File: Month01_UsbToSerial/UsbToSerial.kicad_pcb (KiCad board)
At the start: 2 copper layers, 14 parts, among them J1 USB_B_Micro, J2 Conn1, J3 Conn2, U1 FT232RL

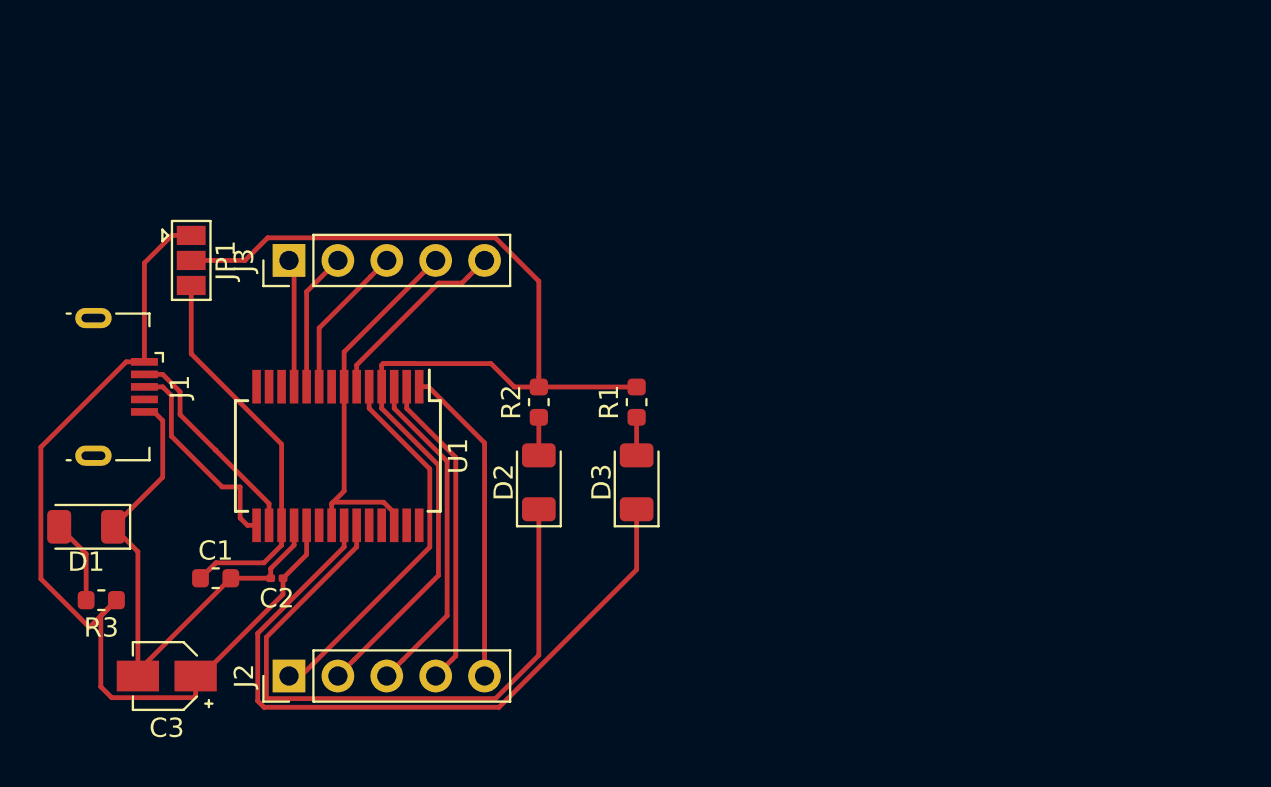
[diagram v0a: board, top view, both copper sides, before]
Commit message: added files from mistaken working copy in separate folder
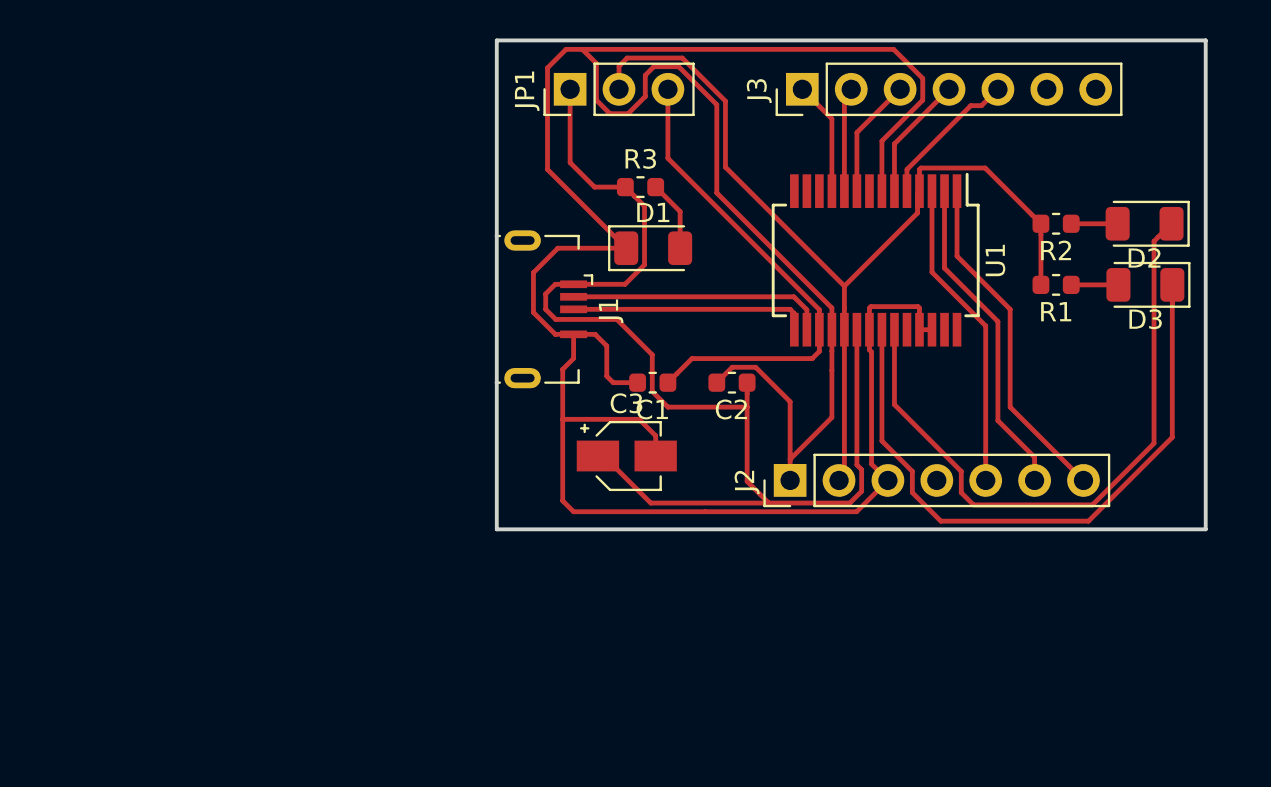
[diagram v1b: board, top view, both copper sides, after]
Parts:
- C2: footprint Capacitor_SMD:C_0201_0603Metric -> Capacitor_SMD:C_0603_1608Metric
- J2: value Conn1 -> Conn_01x07_Female; footprint Connector_PinHeader_2.54mm:PinHeader_1x05_P2.54mm_Vertical -> Connector_PinHeader_2.54mm:PinHeader_1x07_P2.54mm_Vertical
- J3: value Conn2 -> Conn_01x07_Female; footprint Connector_PinHeader_2.54mm:PinHeader_1x05_P2.54mm_Vertical -> Connector_PinHeader_2.54mm:PinHeader_1x07_P2.54mm_Vertical
- JP1: footprint Jumper:SolderJumper-3_P1.3mm_Open_Pad1.0x1.5mm -> Connector_PinHeader_2.54mm:PinHeader_1x03_P2.54mm_Vertical
- moved R3 35.3 mm to (84.3, 74.9), turned to 0 degrees
- moved D2 34.2 mm to (110.5, 76.8), turned to 180 degrees
- moved D1 32.8 mm to (85.0, 78.1), turned to 0 degrees
- moved U1 29.7 mm to (96.5, 78.7)
- moved R2 28.4 mm to (105.9, 76.8), turned to 180 degrees
- moved D3 28.3 mm to (110.5, 80.0), turned to 180 degrees
- moved J3 28.1 mm to (92.7, 69.8)
- moved J2 27.9 mm to (92.1, 90.2)
- moved C3 26.5 mm to (83.6, 88.9), turned to 0 degrees
- moved C2 25.7 mm to (89.1, 85.1)
- moved C1 24.9 mm to (84.9, 85.1), turned to 180 degrees
- moved J1 22.7 mm to (79.4, 81.3)
- moved R1 22.6 mm to (105.9, 80.0), turned to 180 degrees
- moved JP1 21.6 mm to (80.6, 69.8), turned to 90 degrees
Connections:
- J2 pad 1: RXI -> GNDREF
- J2 pad 3: RTS -> GNDREF
- J2 pad 4: DTR -> Net-(J2-Pad4)
- J2 pad 5: TX0 -> RTS
- J3 pad 4: GNDREF -> RI
- J3 pad 5: RI -> RXI
- U1 pad 19: +5V -> PWR
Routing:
- net GNDREF: track 48.5 -> 143.0 mm
- net +5V: track 49.2 -> 62.1 mm
- net RXI: track 19.7 -> 7.58 mm
- net PWR: track 59.9 -> 48.6 mm
- net +3V3: track 20.4 -> 25.4 mm
- net Net-(D3-Pad1): track 36.9 -> 33.0 mm
- net RI: track 10.0 -> 6.46 mm
- net Net-(J1-Pad2): track 11.1 -> 13.4 mm
- net DCD: track 7.23 -> 5.44 mm
- net DCR: track 8.02 -> 6.22 mm
- net Net-(J1-Pad3): track 11.0 -> 12.4 mm
- net RTS: track 17.5 -> 16.2 mm
- net TX0: track 16.7 -> 17.8 mm
- net CTS: track 6.67 -> 5.93 mm
- net Net-(D1-Pad2): track 4.39 -> 3.70 mm
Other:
- board outline added: 36.8 x 25.4 mm

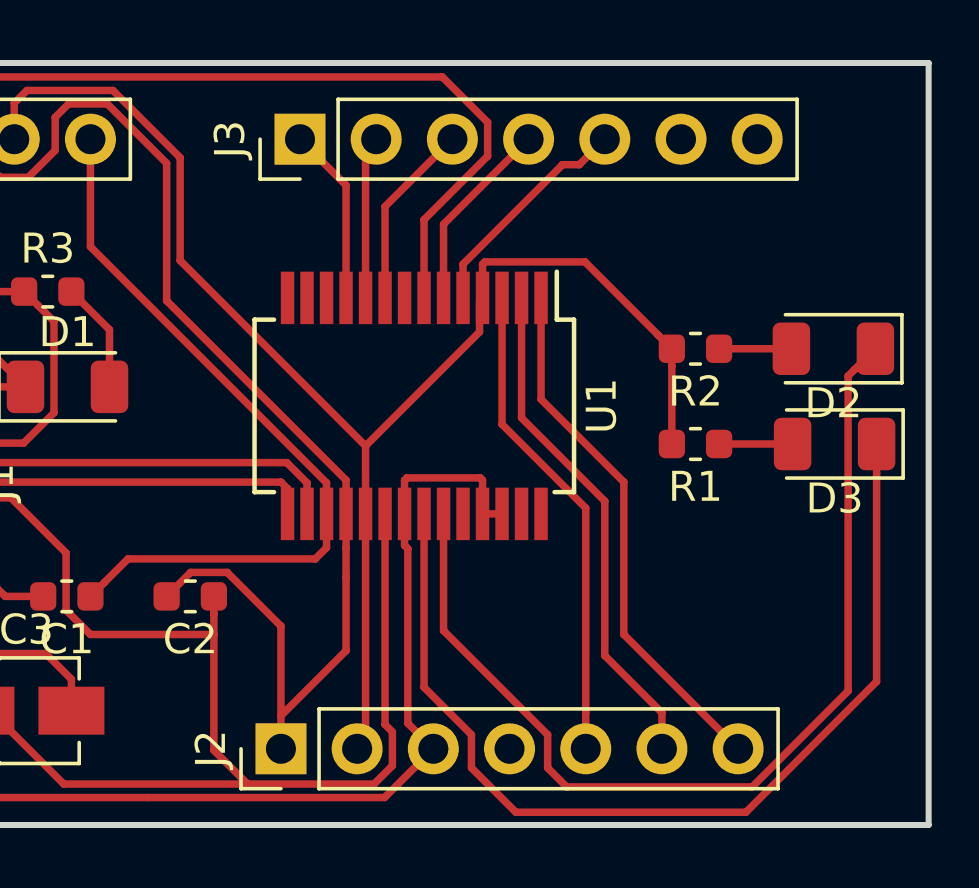
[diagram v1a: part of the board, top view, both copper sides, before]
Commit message: Corrected position of the headers as I misplaced the connector
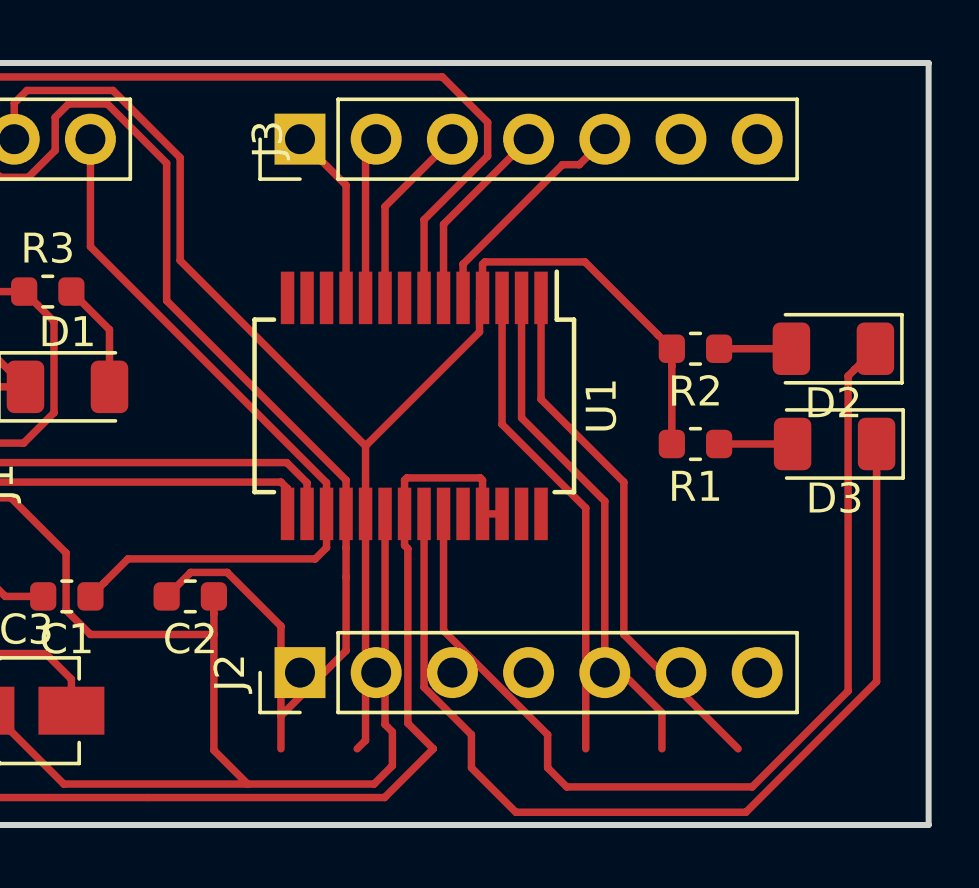
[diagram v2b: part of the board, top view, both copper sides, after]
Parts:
- moved J2 2.62 mm to (92.7, 87.6)
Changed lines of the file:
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@@
-(kicad_pcb (version 20171130) (host pcbnew "(5.0.1)-3")
+(kicad_pcb (version 20171130) (host pcbnew "(5.1.2)-2")
   (general
     (thickness 1.6)
@@
     (zone_45_only no)
     (trace_min 0.2)
-    (segment_width 0.2)
-    (edge_width 0.15)
     (via_size 0.8)
     (via_drill 0.4)
@@
     (uvia_min_size 0.2)
     (uvia_min_drill 0.1)
+    (edge_width 0.15)
+    (segment_width 0.2)
     (pcb_text_width 0.3)
     (pcb_text_size 1.5 1.5)
@@
   )
   (module Connector_PinHeader_2.54mm:PinHeader_1x07_P2.54mm_Vertical (layer F.Cu)
-    (at 92.075 90.17 90)
+    (at 92.71 87.63 90)
     (descr "Through hole straight pin header, 1x07, 2.54mm pitch, single row")
     (tags "Through hole pin header THT 1x07 2.54mm single row")
@@
     (descr "Through hole straight pin header, 1x07, 2.54mm pitch, single row")
     (tags "Through hole pin header THT 1x07 2.54mm single row")
-    (fp_text reference J3 (at 0 -2.33 90) (layer F.SilkS)
-      (effects (font (size 1 1) (thickness 0.15)))
-    )
+    (fp_text reference J3 (at 0 -1.067501 90) (layer F.SilkS)
+      (effects (font (size 1 1) (thickness 0.15)))
+    )

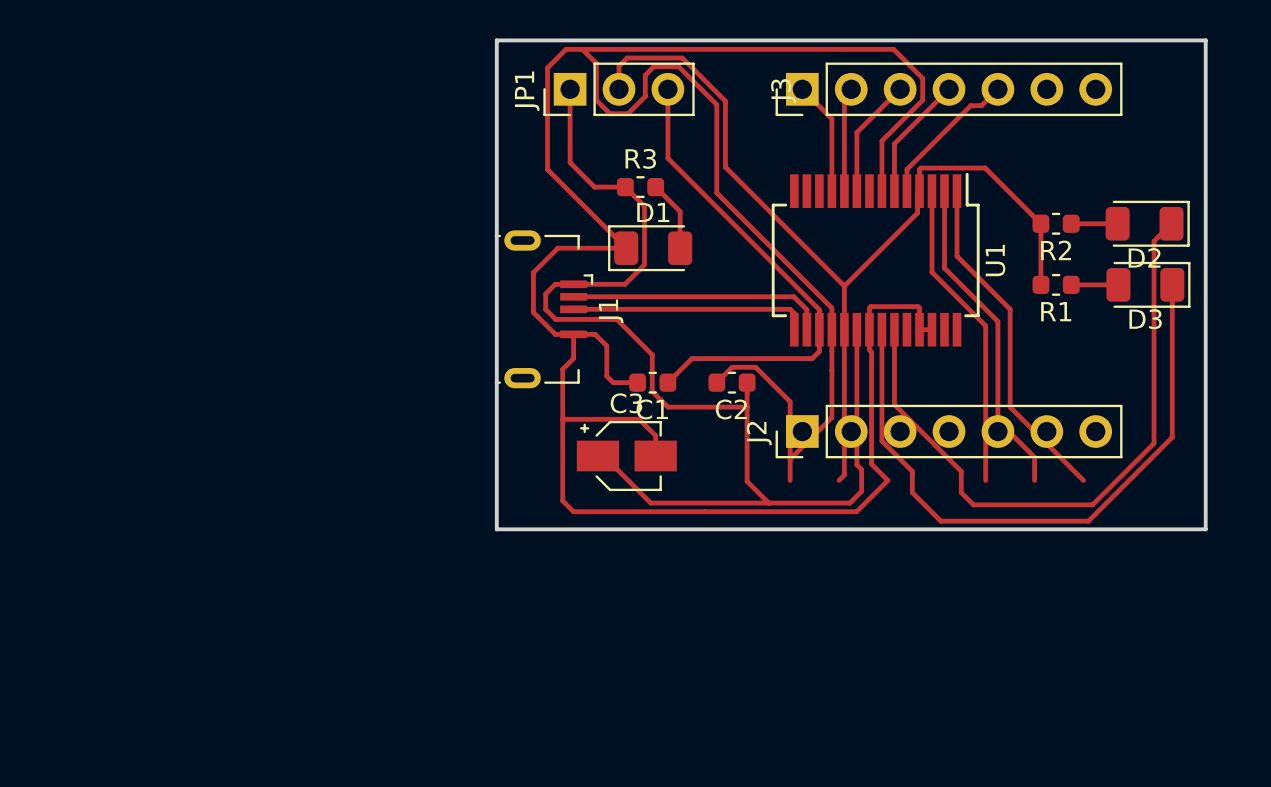
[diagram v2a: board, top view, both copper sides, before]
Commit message: updated usbtoSerial.kicad_pcb with corrected layout
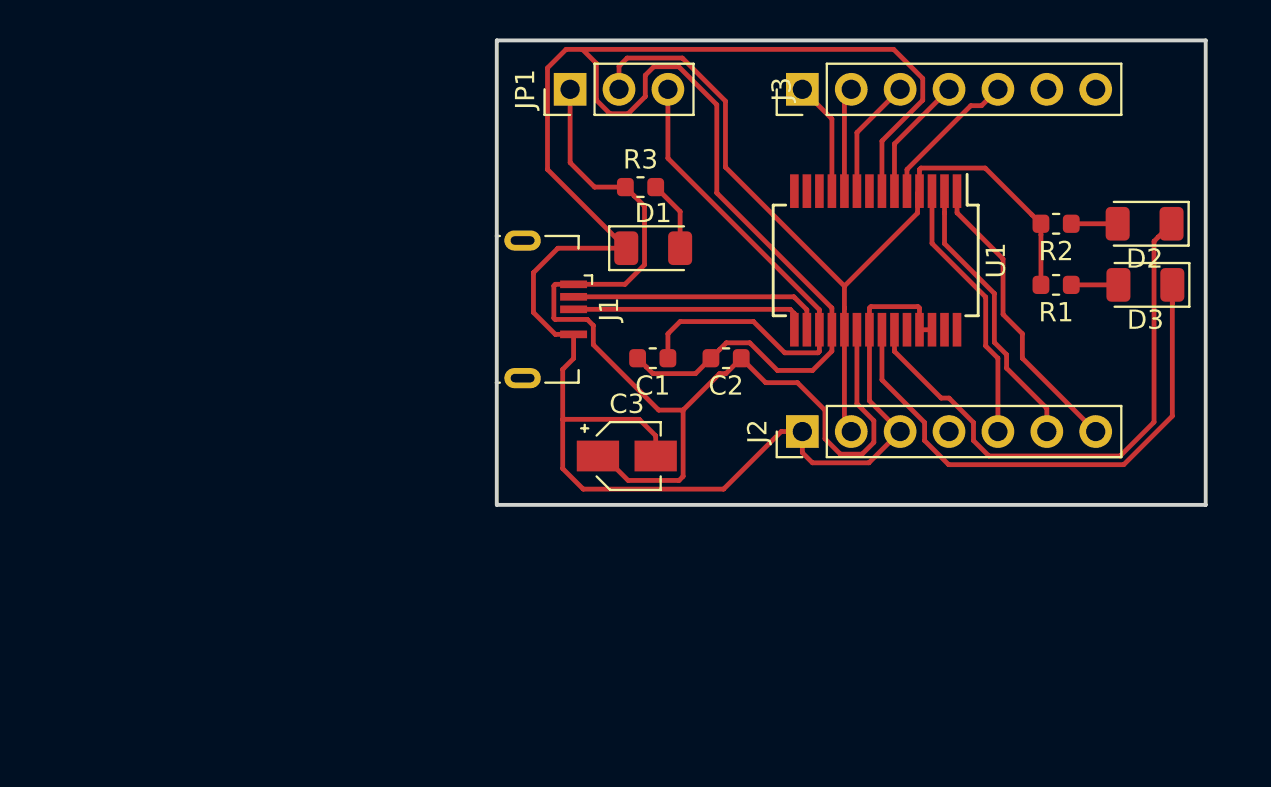
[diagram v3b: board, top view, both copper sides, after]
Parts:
- C3: value 10uF -> (none)
- moved C2 1.31 mm to (88.7, 83.8)
- moved C1 1.27 mm to (84.9, 83.8)
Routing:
- net GNDREF: track 143.0 -> 133.8 mm
- net +5V: track 62.1 -> 56.7 mm
- net Net-(D3-Pad1): track 33.0 -> 27.9 mm
- net Net-(D2-Pad1): track 33.3 -> 28.8 mm
- net PWR: track 48.6 -> 46.1 mm
- net DTR: track 17.0 -> 14.7 mm
- net TX0: track 17.8 -> 15.5 mm
- net RTS: track 16.2 -> 13.9 mm
- net +3V3: track 25.4 -> 27.0 mm
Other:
- board size 36.8 x 25.4 mm -> 36.8 x 24.1 mm
